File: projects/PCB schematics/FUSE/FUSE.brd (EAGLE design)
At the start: 487.7 x 352.7 mm, 111 parts, among them J1 178328-2, J2 178328-2, J3 178328-2, J4 178328-2, J5 178328-2, J6 178328-2, J7 178328-2, J8 178328-2, J9 178328-2, X1 5566-20, X10 5566-20, X11 5566-20, X2 5566-20, X3 5566-20, X4 5566-20, X5 5566-20, X6 5566-20, X7 5566-20, X8 5566-20, X9 D1200D-20

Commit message: FUSE - Initial draft.
Squash - Highly Irrelevant update
Reason for commit: Couldn't figure out how to squash minor update into a big one.

Squash - FUSE - Initial draft done.

Board has been made for 24 fused connections. 4 of these will be needed, but the design can be repeated.

Silkscreen is the only thing to be edited.

Squash - FUSE - Minor tweaks.
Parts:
- removed F25, F26, F27, F28, F29, F30, F31, F32, F33, F34, F35, F36, F37, F38, F39, F40, F41, F42, F43, F44, F45, F46, F47, F48, F49, F50, F51, F52, F53, F54, F55, F56, F57, F58, F59, F60, F61, F62, F63, F64, F65, F66, F67, F68, F69, F70, F71, F72, F73, F74, F75, F76, F77, F78, F79, F80, F81, F82, F83, F84, F85, F86, F87, F88, F89, F90, F91: 0885001.DR, 0885001.DR:FUSC10948X488N
- removed J3, J4, J5, J6, J7, J8, J9: 178328-2, 178328-2:178328-2
- removed X1, X10, X11, X2, X3, X4, X5, X6, X7, X8: 5566-20, con-molex:5566-20
- removed X9: D1200D-20, con-tyco:D1200D-20
- J1, J2: value 178328-2 -> 24P(90DEG)_1-794108-0; device 178328-2:178328-2 -> con-MATE-N-LOK:CON24_2X12_P4_14MM_RAMNL
- moved F23 781.1 mm to (38.1, 15.2), turned to 90 degrees
- moved F22 776.3 mm to (30.5, 15.2), turned to 90 degrees
- moved F21 771.5 mm to (22.9, 15.2), turned to 90 degrees
- moved F4 765.2 mm to (30.5, 67.3), turned to 270 degrees
- moved F24 747.8 mm to (45.7, 15.2), turned to 90 degrees
- moved F1 676.1 mm to (7.62, 67.3), turned to 270 degrees
- moved F14 669.4 mm to (15.2, 33.0), turned to 270 degrees
- moved F20 669.1 mm to (15.2, 15.2), turned to 90 degrees
- moved F7 668.3 mm to (7.62, 50.8), turned to 90 degrees
- moved F2 667.2 mm to (15.2, 67.3), turned to 270 degrees
- moved F3 664.8 mm to (22.9, 67.3), turned to 270 degrees
- moved F13 664.5 mm to (7.62, 33.0), turned to 270 degrees
- moved F19 664.2 mm to (7.62, 15.2), turned to 90 degrees
- moved F8 659.2 mm to (15.2, 50.8), turned to 90 degrees
- moved F16 653.1 mm to (30.5, 33.0), turned to 270 degrees
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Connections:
- removed net INPUT25: F45.1, J3.A9, X3.5
- removed net INPUT26: F46.1, J3.B1, X3.6
- removed net INPUT27: F47.1, J3.B3, X3.7
- removed net INPUT28: F48.1, J3.B5, X3.8
- removed net INPUT29: F49.1, J3.B7, X3.9
- removed net INPUT30: F50.1, J3.B9, X3.10
- removed net INPUT31: F11.1, J4.A1, X3.11
- removed net INPUT32: F12.1, J4.A3, X3.12
- removed net INPUT33: F13.1, J4.A5, X3.13
- removed net INPUT34: F14.1, J4.A7, X3.14
- removed net INPUT35: F15.1, J4.A9, X3.15
- removed net INPUT36: F16.1, J4.B1, X3.16
- removed net INPUT37: F17.1, J4.B3, X3.17
- removed net INPUT38: F18.1, J4.B5, X3.18
- removed net INPUT39: F19.1, J4.B7, X3.19
- removed net INPUT40: F20.1, J4.B9, X3.20
- removed net INPUT41: F31.1, J5.A1, X4.1
- removed net INPUT42: F32.1, J5.A3, X4.2
- removed net INPUT43: F33.1, J5.A5, X4.3
- removed net INPUT44: F34.1, J5.A7, X4.4
- removed net INPUT45: F35.1, J5.A9, X4.5
- removed net INPUT46: F36.1, J5.B1, X4.6
- removed net INPUT47: F37.1, J5.B3, X4.7
- removed net INPUT48: F38.1, J5.B5, X4.8
- removed net INPUT49: F39.1, J5.B7, X4.9
- removed net INPUT50: F40.1, J5.B9, X4.10
- removed net INPUT51: F51.1, J6.A1, X4.11
- removed net INPUT52: F52.1, J6.A3, X4.12
- removed net INPUT53: F53.1, J6.A5, X4.13
- removed net INPUT54: F54.1, J6.A7, X4.14
- removed net INPUT55: F55.1, J6.A9, X4.15
- removed net INPUT56: F56.1, J6.B1, X4.16
- removed net INPUT57: F57.1, J6.B3, X4.17
- removed net INPUT58: F58.1, J6.B5, X4.18
- removed net INPUT59: F59.1, J6.B7, X4.19
- removed net INPUT60: F60.1, J6.B9, X4.20
- removed net INPUT61: F61.1, J7.A1, X5.1
- removed net INPUT62: F62.1, J7.A3, X5.2
- removed net INPUT63: F63.1, J7.A5, X5.3
- removed net INPUT64: F64.1, J7.A7, X5.4
- removed net INPUT65: F65.1, J7.A9, X5.5
- removed net INPUT66: F66.1, J7.B1, X5.6
- removed net INPUT67: F67.1, J7.B3, X5.7
- removed net INPUT68: F68.1, J7.B5, X5.8
- removed net INPUT69: F69.1, J7.B7, X5.9
- removed net INPUT70: F70.1, J7.B9, X5.10
- removed net INPUT71: F71.1, J8.A1, X5.11
- removed net INPUT72: F72.1, J8.A3, X5.12
- removed net INPUT73: F73.1, J8.A5, X5.13
- removed net INPUT74: F74.1, J8.A7, X5.14
- removed net INPUT75: F75.1, J8.A9, X5.15
- removed net INPUT76: F76.1, J8.B1, X5.16
- removed net INPUT77: F77.1, J8.B3, X5.17
- removed net INPUT78: F78.1, J8.B5, X5.18
- removed net INPUT79: F79.1, J8.B7, X5.19
- removed net INPUT80: F80.1, J8.B9, X5.20
- removed net INPUT81: F81.1, J9.A1, X10.1
- removed net INPUT82: F82.1, J9.A3, X10.2
- removed net INPUT83: F83.1, J9.A5, X10.3
- removed net INPUT84: F84.1, J9.A7, X10.4
- removed net INPUT85: F85.1, J9.A9, X10.5
- removed net INPUT86: F86.1, J9.B1, X10.6
- removed net INPUT87: F87.1, J9.B3, X10.7
- removed net INPUT88: F88.1, J9.B5, X10.8
- removed net INPUT89: F89.1, J9.B7, X10.9
- removed net INPUT90: F90.1, J9.B9, X10.10
- removed net INPUT91: F91.1, X10.11
- removed net OUTPUT25: F45.2, X6.5
- removed net OUTPUT26: F46.2, X6.6
- removed net OUTPUT27: F47.2, X6.7
- removed net OUTPUT28: F48.2, X6.8
- removed net OUTPUT29: F49.2, X6.9
- removed net OUTPUT30: F50.2, X6.10
- removed net OUTPUT31: F11.2, X6.11
- removed net OUTPUT32: F12.2, X6.12
- removed net OUTPUT33: F13.2, X6.13
- removed net OUTPUT34: F14.2, X6.14
- removed net OUTPUT35: F15.2, X6.15
- removed net OUTPUT36: F16.2, X6.16
- removed net OUTPUT37: F17.2, X6.17
- removed net OUTPUT38: F18.2, X6.18
- removed net OUTPUT39: F19.2, X6.19
- removed net OUTPUT40: F20.2, X6.20
- removed net OUTPUT41: F31.2, F61.2, X7.1
- removed net OUTPUT42: F32.2, X7.2
- removed net OUTPUT43: F33.2, X7.3
- removed net OUTPUT44: F34.2, X7.4
- removed net OUTPUT45: F35.2, X7.5
- removed net OUTPUT46: F36.2, X7.6
- removed net OUTPUT47: F37.2, X7.7
- removed net OUTPUT48: F38.2, X7.8
- removed net OUTPUT49: F39.2, X7.9
- removed net OUTPUT50: F40.2, X7.10
- removed net OUTPUT51: F51.2, X7.11
- removed net OUTPUT52: F52.2, X7.12
- removed net OUTPUT53: F53.2, X7.13
- removed net OUTPUT54: F54.2, X7.14
- removed net OUTPUT55: F55.2, X7.15
- removed net OUTPUT56: F56.2, X7.16
- removed net OUTPUT57: F57.2, X7.17
- removed net OUTPUT58: F58.2, X7.18
- removed net OUTPUT59: F59.2, X7.19
- removed net OUTPUT60: F60.2, X7.20
- removed net OUTPUT61: X8.1
- removed net OUTPUT62: F62.2, X8.2
- removed net OUTPUT63: F63.2, X8.3
- removed net OUTPUT64: F64.2, X8.4
- removed net OUTPUT65: F65.2, X8.5
- removed net OUTPUT66: F66.2, X8.6
- removed net OUTPUT67: F67.2, X8.7
- removed net OUTPUT68: F68.2, X8.8
- removed net OUTPUT69: F69.2, X8.9
- removed net OUTPUT70: F70.2, X8.10
- removed net OUTPUT71: F71.2, X8.11
- removed net OUTPUT72: F72.2, X8.12
- removed net OUTPUT73: F73.2, X8.13
- removed net OUTPUT74: F74.2, X8.14
- removed net OUTPUT75: F75.2, X8.15
- removed net OUTPUT76: F76.2, X8.16
- removed net OUTPUT77: F77.2, X8.17
- removed net OUTPUT78: F78.2, X8.18
- removed net OUTPUT79: F79.2, X8.19
- removed net OUTPUT80: F80.2, X8.20
- removed net OUTPUT81: F81.2, X11.1
- removed net OUTPUT82: F82.2, X11.2
- removed net OUTPUT83: F83.2, X11.3
- removed net OUTPUT84: F84.2, X11.4
- removed net OUTPUT85: F85.2, X11.5
- removed net OUTPUT86: F86.2, X11.6
- removed net OUTPUT87: F87.2, X11.7
- removed net OUTPUT88: F88.2, X11.8
- removed net OUTPUT89: F89.2, X11.9
- removed net OUTPUT90: F90.2, X11.10
- removed net OUTPUT91: F91.2, X11.11
- removed net OUTPUT\4: F4.2
- net INPUT1: now also J1.1; no longer J1.A1, X1.1
- net INPUT10: now also J1.10; no longer J1.B9, X1.10
- net INPUT11: now also F11.1, J1.11; no longer F21.1, J2.A1, X1.11
- net INPUT12: now also F12.1, J1.12; no longer F22.1, J2.A3, X1.12
- net INPUT13: now also F13.1, J1.13; no longer F23.1, J2.A5, X1.13
- net INPUT14: now also F14.1, J1.14; no longer F24.1, J2.A7, X1.14
- net INPUT15: now also F15.1, J1.15; no longer F25.1, J2.A9, X1.15
- net INPUT16: now also F16.1, J1.16; no longer F26.1, J2.B1, X1.16
- net INPUT17: now also F17.1, J1.17; no longer F27.1, J2.B3, X1.17
- net INPUT18: now also F18.1, J1.18; no longer F28.1, J2.B5, X1.18
- net INPUT19: now also F19.1, J1.19; no longer F29.1, J2.B7, X1.19
- net INPUT2: now also J1.2; no longer J1.A3, X1.2
- net INPUT20: now also F20.1, J1.20; no longer F30.1, J2.B9, X1.20
- net INPUT21: now also F21.1, J1.21; no longer F41.1, J3.A1, X3.1
- net INPUT22: now also F22.1, J1.22; no longer F42.1, J3.A3, X3.2
- net INPUT23: now also F23.1, J1.23; no longer F43.1, J3.A5, X3.3
- net INPUT24: now also F24.1, J1.24; no longer F44.1, J3.A7, X3.4
- net INPUT3: now also J1.3; no longer J1.A5, X1.3
- net INPUT4: now also J1.4; no longer J1.A7, X1.4
- net INPUT5: now also J1.5; no longer J1.A9, X1.5
- net INPUT6: now also J1.6; no longer J1.B1, X1.6
- net INPUT7: now also J1.7; no longer J1.B3, X1.7
- net INPUT8: now also J1.8; no longer J1.B5, X1.8
- net INPUT9: now also J1.9; no longer J1.B7, X1.9
- net OUTPUT1: now also J2.1; no longer X2.1
- net OUTPUT10: now also J2.10; no longer X2.10
- net OUTPUT11: now also F11.2, J2.11; no longer F21.2, X2.11
- net OUTPUT12: now also F12.2, J2.12; no longer F22.2, X2.12
- net OUTPUT13: now also F13.2, J2.13; no longer F23.2, X2.13
- net OUTPUT14: now also F14.2, J2.14; no longer F24.2, X2.14
- net OUTPUT15: now also F15.2, J2.15; no longer F25.2, X2.15
- net OUTPUT16: now also F16.2, J2.16; no longer F26.2, X2.16
- net OUTPUT17: now also F17.2, J2.17; no longer F27.2, X2.17
- net OUTPUT18: now also F18.2, J2.18; no longer F28.2, X2.18
- net OUTPUT19: now also F19.2, J2.19; no longer F29.2, X2.19
- net OUTPUT2: now also J2.2; no longer X2.2
- net OUTPUT20: now also F20.2, J2.20; no longer F30.2, X2.20
- net OUTPUT21: now also F21.2, J2.21; no longer F41.2, X6.1
- net OUTPUT22: now also F22.2, J2.22; no longer F42.2, X6.2
- net OUTPUT23: now also F23.2, J2.23; no longer F43.2, X6.3
- net OUTPUT24: now also F24.2, J2.24; no longer F44.2, X6.4
- net OUTPUT3: now also J2.3; no longer X2.3
- net OUTPUT4: now also F4.2, J2.4; no longer X2.4
- net OUTPUT5: now also J2.5; no longer X2.5
- net OUTPUT6: now also J2.6; no longer X2.6
- net OUTPUT7: now also J2.7; no longer X2.7
- net OUTPUT8: now also J2.8; no longer X2.8
- net OUTPUT9: now also J2.9; no longer X2.9
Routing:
- net INPUT57: track 1472.9 -> 0.00 mm
- net INPUT51: track 1424.3 -> 0.00 mm
- net INPUT56: track 1332.0 -> 0.00 mm
- net INPUT53: track 1318.2 -> 0.00 mm
- net INPUT54: track 1305.1 -> 0.00 mm
- net INPUT55: track 937.2 -> 0.00 mm, vias 18 -> 0
- net INPUT29: track 935.2 -> 0.00 mm, vias 7 -> 0
- net INPUT43: track 918.9 -> 0.00 mm, vias 7 -> 0
- net INPUT87: track 904.5 -> 0.00 mm, vias 22 -> 0
- net INPUT59: track 888.9 -> 0.00 mm, vias 10 -> 0
- net INPUT49: track 882.4 -> 0.00 mm, vias 7 -> 0
- net INPUT60: track 871.5 -> 0.00 mm, vias 14 -> 0
- net INPUT42: track 871.1 -> 0.00 mm, vias 18 -> 0
- net INPUT58: track 861.9 -> 0.00 mm, vias 15 -> 0
- net INPUT89: track 858.9 -> 0.00 mm, vias 15 -> 0
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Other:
- board size 487.7 x 352.7 mm -> 71.1 x 99.1 mm
- board text added: "1"

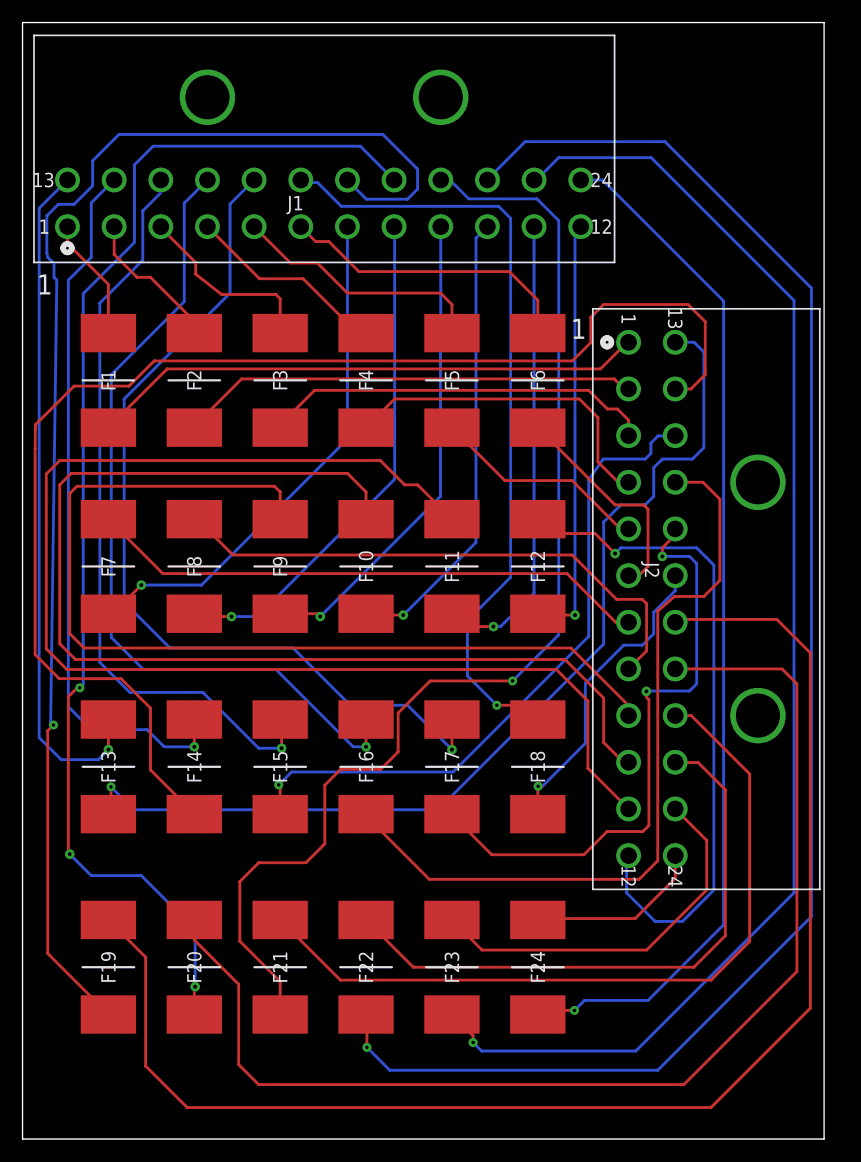
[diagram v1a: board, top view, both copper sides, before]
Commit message: FUSE - Pull request #4.
Squash - FUSE - PR#4 changes.

Minor changes made in trace placement.
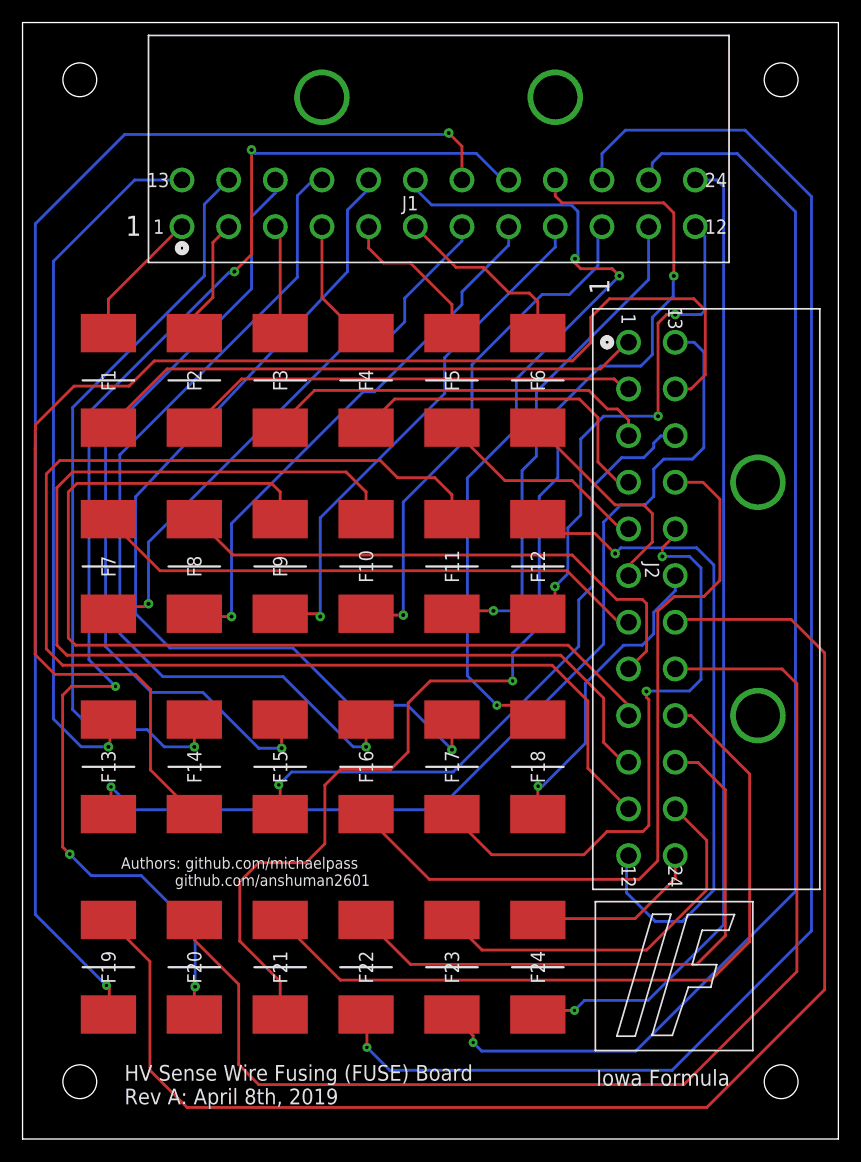
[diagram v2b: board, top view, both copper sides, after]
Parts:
- moved J1 10.2 mm to (59.7, 85.1)
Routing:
- net INPUT6: track 26.7 -> 16.4 mm
- net INPUT20: track 110.2 -> 119.6 mm, vias 3 -> 5
- net INPUT5: track 23.0 -> 13.9 mm
- net INPUT21: track 104.5 -> 112.5 mm, vias 1 -> 2
- net INPUT12: track 38.0 -> 45.4 mm, vias 1 -> 3
- net INPUT3: track 16.8 -> 9.66 mm
- net INPUT4: track 18.0 -> 11.5 mm
- net INPUT10: track 40.9 -> 46.5 mm
- net INPUT7: track 46.5 -> 50.8 mm
- net INPUT23: track 119.5 -> 115.3 mm
- net INPUT24: track 92.3 -> 88.1 mm
- net INPUT9: track 42.7 -> 46.9 mm
- net INPUT18: track 70.1 -> 74.0 mm, vias 1 -> 3
- net INPUT14: track 63.5 -> 67.3 mm
- net INPUT19: track 121.3 -> 117.6 mm, vias 1 -> 2
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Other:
- board size 71.1 x 99.1 mm -> 72.4 x 99.1 mm
- board text added: "Authors: github.com/michaelpass github.com/anshuman2601"
- board text added: "HV Sense Wire Fusing (FUSE) Board Rev A: April 8th, 2019"
- board text added: "Iowa Formula"

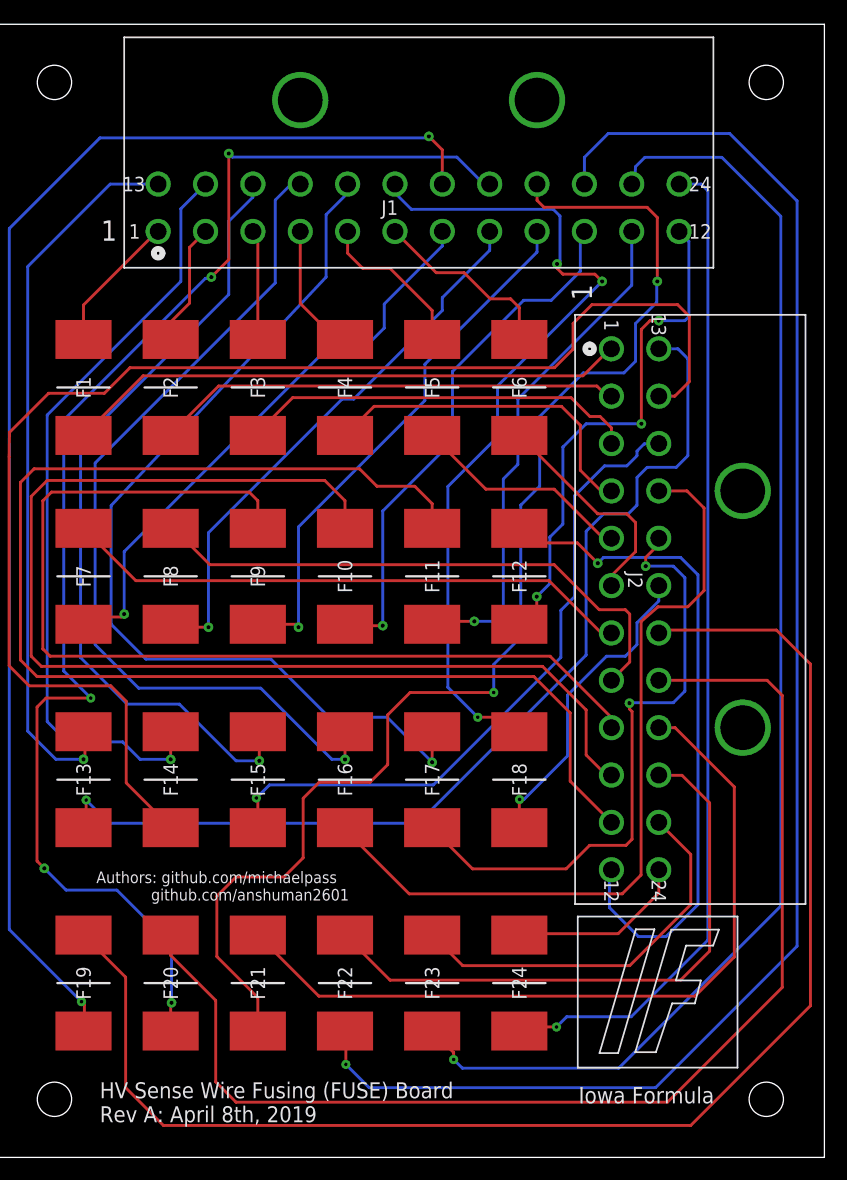
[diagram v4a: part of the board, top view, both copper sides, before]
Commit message: PROJ - Silkscreen modifications - 50%.
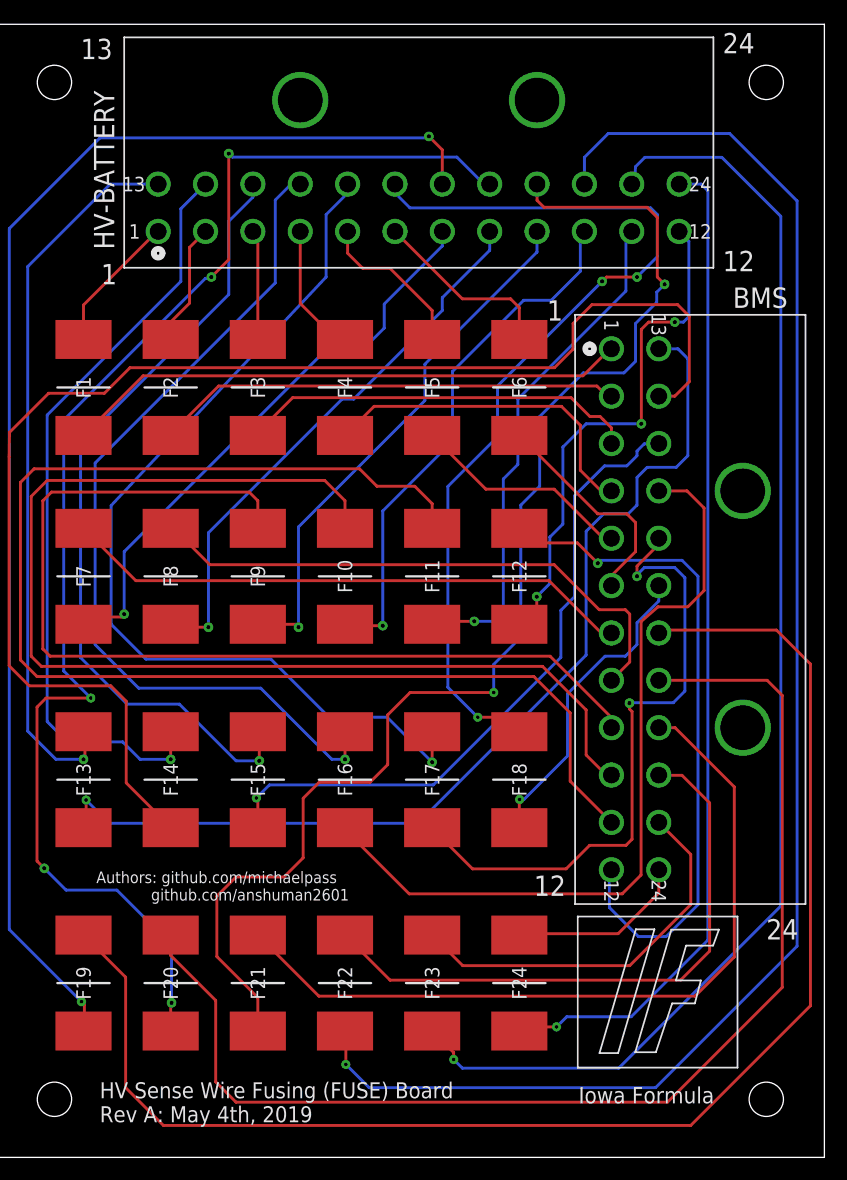
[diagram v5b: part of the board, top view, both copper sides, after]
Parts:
- renumbered J1 to HV-BATTERY, J2 to BMS
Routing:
- net INPUT18: track 74.0 -> 82.8 mm
- net OUTPUT17: track 54.0 -> 56.3 mm
- net INPUT21: track 112.5 -> 113.1 mm
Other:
- board text added: "12"
- board text added: "13"
- board text added: "24"
- board text added: "HV Sense Wire Fusing (FUSE) Board Rev A: May 4th, 2019"
- board text removed: "HV Sense Wire Fusing (FUSE) Board Rev A: April 8th, 2019"

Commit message: PROJ - Gerber files major milestone - 05/05/19.
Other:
- board text added: "HV Sense Wire Fusing (FUSE) Board Rev A: May 5th, 2019"
- board text removed: "HV Sense Wire Fusing (FUSE) Board Rev A: May 4th, 2019"
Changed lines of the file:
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@@
 <text x="50.9016" y="4.7244" size="1.4224" layer="25" font="vector">Iowa Formula</text>
 <text x="9.0424" y="3.0734" size="1.397" layer="25">HV Sense Wire Fusing (FUSE) Board
-Rev A: May 4th, 2019</text>
+Rev A: May 5th, 2019</text>
 <text x="8.7376" y="22.4536" size="1.016" layer="25" font="vector">Authors: github.com/michaelpass
             github.com/anshuman2601             </text>
@@
 <wire x1="71.1708" y1="13.2588" x2="71.1708" y2="43.1292" width="0.254" layer="1"/>
 </signal>
-<signal name="N$48">
-</signal>
 <signal name="INPUT2">
